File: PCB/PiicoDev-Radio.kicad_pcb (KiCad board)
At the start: 2 copper layers, 25.4 x 52 mm, 32 parts, among them J1 , J2 , J3 Conn_01x05_Male, SW1 ADDR, U1 ATtiny1616-M, U2 RFM69HCW

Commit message: Change R5 to 1k
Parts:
- R5: value 510R -> 1k
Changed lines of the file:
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@@
   (net 27 "Net-(D2-Pad2)")
   (net 28 "Net-(JP1-Pad1)")
-  (net 29 "Net-(AE2-Pad1)")
+  (net 29 "Net-(AE1-Pad1)")
   (net 30 "/RF2")
   (net 31 "/RF1")
@@
     (property "Sheetfile" "PiicoDev-Radio.kicad_sch")
     (property "Sheetname" "")
+    (property "exclude_from_bom" "")
     (clearance 1.2)
-    (attr exclude_from_pos_files)
+    (attr exclude_from_pos_files exclude_from_bom)
     (fp_text reference "H1" (at 0 -3.7) (layer "F.SilkS") hide
       (effects (font (size 1 1) (thickness 0.15)))
@@
     (property "Sheetfile" "PiicoDev-Radio.kicad_sch")
     (property "Sheetname" "")
-    (attr smd)
+    (property "exclude_from_bom" "")
+    (attr smd exclude_from_bom)
     (fp_text reference "FID1" (at 0 -2) (layer "F.Fab") hide
       (effects (font (size 1 1) (thickness 0.15)))
@@
     (property "Sheetfile" "PiicoDev-Radio.kicad_sch")
     (property "Sheetname" "")
+    (property "exclude_from_bom" "")
     (clearance 1.2)
-    (attr exclude_from_pos_files)
+    (attr exclude_from_pos_files exclude_from_bom)
     (fp_text reference "H2" (at 0 -3.7) (layer "F.SilkS") hide
       (effects (font (size 1 1) (thickness 0.15)))
@@
     (property "Sheetfile" "PiicoDev-Radio.kicad_sch")
     (property "Sheetname" "")
-    (attr smd)
+    (property "exclude_from_bom" "")
+    (attr smd exclude_from_bom)
     (fp_text reference "FID2" (at 0 -2) (layer "F.Fab") hide
       (effects (font (size 1 1) (thickness 0.15)))
@@
     (property "Sheetfile" "PiicoDev-Radio.kicad_sch")
     (property "Sheetname" "")
-    (attr through_hole)
+    (property "exclude_from_bom" "")
+    (attr through_hole exclude_from_bom)
     (fp_text reference "LOGO1" (at 0 0) (layer "F.Fab") hide
       (effects (font (size 1.524 1.524) (thickness 0.3)))
@@
     (property "Sheetfile" "PiicoDev-Radio.kicad_sch")
     (property "Sheetname" "")
-    (attr through_hole)
+    (property "exclude_from_bom" "")
+    (attr through_hole exclude_from_bom)
     (fp_text reference "G1" (at 0 0) (layer "F.SilkS") hide
       (effects (font (size 1.524 1.524) (thickness 0.3)))
@@
       (effects (font (size 1 1) (thickness 0.15)))
     )
-    (fp_text value "510R" (at 0.9652 0.3556) (layer "F.Fab")
+    (fp_text value "1k" (at -0.04 -1.1) (layer "F.Fab")
       (effects (font (size 0.5 0.5) (thickness 0.1)))
     )
@@
     (property "Sheetfile" "PiicoDev-Radio.kicad_sch")
     (property "Sheetname" "")
+    (property "exclude_from_bom" "")
     (clearance 1.2)
-    (attr exclude_from_pos_files)
+    (attr exclude_from_pos_files exclude_from_bom)
     (fp_text reference "H3" (at 0 -3.7) (layer "F.SilkS") hide
       (effects (font (size 1 1) (thickness 0.15)))
@@
     (fp_rect (start -0.8 -0.4) (end 0.8 0.4) (layer "F.Fab") (width 0.1) (fill none))
     (pad "1" smd rect locked (at -0.625 0 270) (size 0.35 0.8) (layers "F.Cu" "F.Paste" "F.Mask")
-      (net 29 "Net-(AE2-Pad1)") (pinfunction "PCB_Trace") (pintype "passive"))
+      (net 29 "Net-(AE1-Pad1)") (pinfunction "PCB_Trace") (pintype "passive"))
     (pad "2,3" smd rect locked (at 0 0.235 270) (size 0.6 0.26) (layers "F.Cu" "F.Paste" "F.Mask"))
     (pad "4" smd rect locked (at 0.625 0 270) (size 0.35 0.8) (layers "F.Cu" "F.Paste" "F.Mask")
@@
     (fp_rect (start 2.025 -0.5) (end 5.625 0.5) (layer "F.Cu") (width 0.01) (fill solid))
     (pad "1" smd rect locked (at 1.53 0 90) (size 1 1) (layers "F.Cu")
-      (net 29 "Net-(AE2-Pad1)") (pinfunction "A") (pintype "input"))
+      (net 29 "Net-(AE1-Pad1)") (pinfunction "A") (pintype "input"))
     (zone (net 0) (net_name "") (layers F&B.Cu) (hatch edge 0.508)
       (connect_pads (clearance 0))
@@
     (property "Sheetfile" "PiicoDev-Radio.kicad_sch")
     (property "Sheetname" "")
-    (attr smd)
+    (property "exclude_from_bom" "")
+    (attr smd exclude_from_bom)
     (fp_text reference "J3" (at 0 -2.75 -90 unlocked) (layer "F.SilkS") hide
       (effects (font (size 1 1) (thickness 0.15)))
@@
     (property "Sheetfile" "PiicoDev-Radio.kicad_sch")
     (property "Sheetname" "")
-    (attr through_hole)
+    (property "exclude_from_bom" "")
+    (attr through_hole exclude_from_bom)
     (fp_text reference "G3" (at 0 0) (layer "B.Fab") hide
       (effects (font (size 1.524 1.524) (thickness 0.3)) (justify mirror))
@@
     (property "Sheetfile" "PiicoDev-Radio.kicad_sch")
     (property "Sheetname" "")
-    (attr exclude_from_pos_files)
+    (property "exclude_from_bom" "")
+    (attr exclude_from_pos_files exclude_from_bom)
     (fp_text reference "JP2" (at 0 1.8 90) (layer "B.Fab") hide
       (effects (font (size 1 1) (thickness 0.15)) (justify mirror))
@@
     (property "Sheetfile" "PiicoDev-Radio.kicad_sch")
     (property "Sheetname" "")
-    (attr through_hole)
+    (property "exclude_from_bom" "")
+    (attr through_hole exclude_from_bom)
     (fp_text reference "G2" (at 0 0) (layer "B.SilkS") hide
       (effects (font (size 1.524 1.524) (thickness 0.3)) (justify mirror))
@@
     (property "Sheetfile" "PiicoDev-Radio.kicad_sch")
     (property "Sheetname" "")
-    (attr exclude_from_pos_files)
+    (property "exclude_from_bom" "")
+    (attr exclude_from_pos_files exclude_from_bom)
     (fp_text reference "JP1" (at 0 1.8 -270) (layer "B.SilkS") hide
       (effects (font (size 1 1) (thickness 0.15)) (justify mirror))

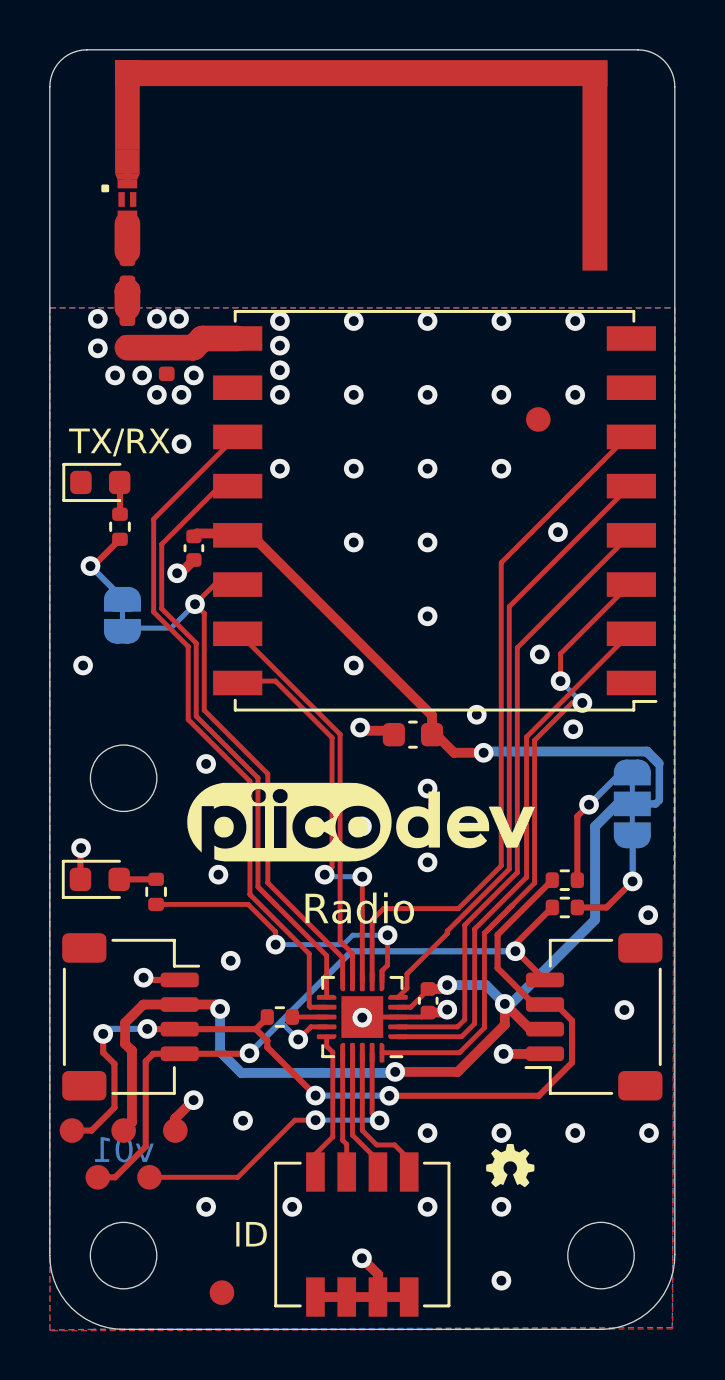
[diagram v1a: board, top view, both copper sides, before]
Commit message: v10 Improve RFM69HCW footprint
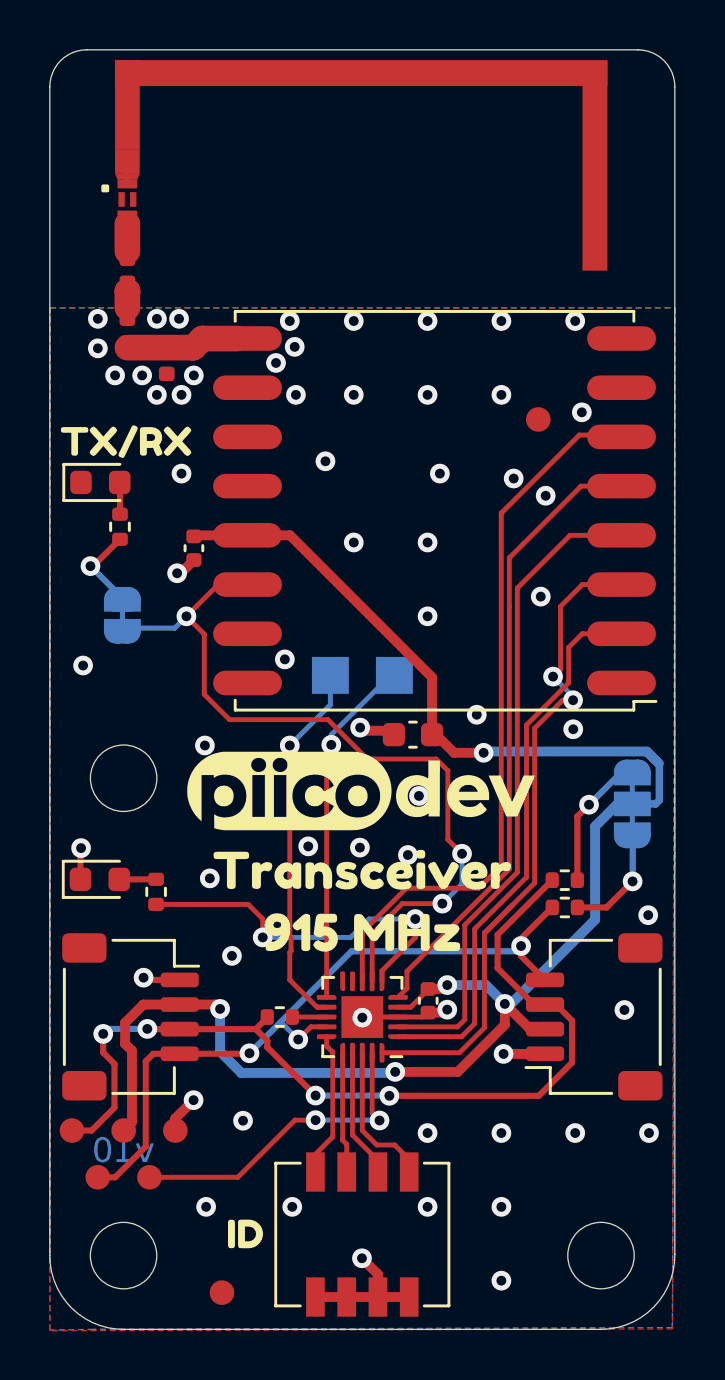
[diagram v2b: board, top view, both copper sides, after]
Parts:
- added TP1: TestPoint, TestPoint:TestPoint_Pad_1.5x1.5mm, B.Cu at (98.6, 87.5)
- added TP2: TestPoint, TestPoint:TestPoint_Pad_1.5x1.5mm, B.Cu at (96.0, 87.5)
- added kibuzzard-637C5B84: G***, kibuzzard-637C5B84, F.Cu at (87.7, 78.0)
- added kibuzzard-637C5BCC: G***, kibuzzard-637C5BCC, F.Cu at (97.3, 95.4)
- added kibuzzard-637C5BDE: G***, kibuzzard-637C5BDE, F.Cu at (97.3, 97.9)
- added kibuzzard-637C5DFB: G***, kibuzzard-637C5DFB, F.Cu at (92.5, 110.2)
- added kibuzzard-637C5EAE: G***, kibuzzard-637C5EAE, B.Cu at (105.6, 92.8)
- added kibuzzard-637C5EDA: G***, kibuzzard-637C5EDA, B.Cu at (97.3, 99.1)
- added kibuzzard-637C5F9F: G***, kibuzzard-637C5F9F, B.Cu at (91.7, 85.0)
- L1: value L -> 4.3n
- L2: value L -> 1nH
- L3: value L -> 10n
- LOGO1: moved to B.Cu
- R5: value 1k -> 10k
- U2: footprint RF_Module:HOPERF_RFM9XW_SMD -> CoreElectronics_Components:HOPERF_RFM69HCW_SMD
- moved LOGO1 6.07 mm to (97.3, 106.7), turned to 180 degrees
- moved G1 1.27 mm to (97.2, 92.3)
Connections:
- U1 pad 10: /DIO0 -> unconnected-(U1-Pad10)
- U1 pad 11: /DIO4 -> /RXD
- U1 pad 12: /DIO3 -> /TXD
- U1 pad 7: /RESET -> /DIO0
- U1 pad 8: /DIO2 -> /RESET
- U1 pad 9: /DIO1 -> unconnected-(U1-Pad9)
- U2 pad 11: /DIO3 -> unconnected-(U2-Pad11)
- U2 pad 12: /DIO4 -> unconnected-(U2-Pad12)
- U2 pad 15: /DIO1 -> unconnected-(U2-Pad15)
- U2 pad 16: /DIO2 -> unconnected-(U2-Pad16)
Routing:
- net /DIO3: track 28.0 -> 0.00 mm
- net /DIO4: track 26.3 -> 0.00 mm
- net /DIO2: track 16.3 -> 0.00 mm, vias 2 -> 0
- net /DIO1: track 16.1 -> 0.00 mm
- net /TXD: track 0.00 -> 15.1 mm, vias 0 -> 1
- net /RXD: track 0.00 -> 14.3 mm, vias 0 -> 1
- net /DIO0: track 23.8 -> 31.9 mm, vias 1 -> 3
- net /PWR_LED: track 12.5 -> 14.9 mm
- net /RESET: track 28.3 -> 29.6 mm
- net +3V3: track 68.6 -> 69.6 mm
- net /SCK: track 25.4 -> 26.4 mm
- net /NSS: track 24.8 -> 25.5 mm
- net /MISO: track 21.9 -> 22.6 mm
- net /MOSI: track 27.7 -> 28.3 mm
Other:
- board text added: "v10"
- board text removed: "I2C PU"
- board text removed: "ID"
- board text removed: "Radio"
- board text removed: "TX/RX"
- board text removed: "TX/RX LED"
- board text removed: "piico.dev/p27"
- board text removed: "v01"
